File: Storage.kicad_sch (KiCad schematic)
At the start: 12 parts, among them U5 KLM4G1FETE-B041

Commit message: changed some ethernet stuff
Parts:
- gave numbers to parts that had none: 1
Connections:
- net EMMC_CMD: now also U1.E16 (PC6/NAND_RB0)
- net EMMC_DQ0: now also U1.B18 (PC8/NAND_DQ0)
- net EMMC_DQ1: now also U1.C17 (PC9/NAND_DQ1)
- net EMMC_DQ2: now also U1.D17 (PC10/NAND_DQ2)
- net EMMC_DQ3: now also U1.C18 (PC11/NAND_DQ3)
- net EMMC_DQ4: now also U1.B17 (PC12/NAND_DQ4)
- net EMMC_DQ5: now also U1.B19 (PC13/NAND_DQ5)
- net EMMC_DQ6: now also U1.F17 (PC14/NAND_DQ6)
- net EMMC_DQ7: now also U1.C19 (PC15/NAND_DQ7)
- net EMMC_RST: now also U1.H16 (PC16/NAND_DQS)
- net at R5.1: now also U1.A17 (PC5/NAND_RE)
- new net SPI0_CLK: U1.B16 (PC2/NAND_CLE)
- new net SPI0_CS: U1.B15 (PC3/NAND_CE1)
- new net SPI0_MISO: U1.C16 (PC1/NAND_ALE)
- new net SPI0_MOSI: U1.C15 (PC0/NAND_WE)
- no-connect marks 127 -> 123
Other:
- moved on the sheet: R5

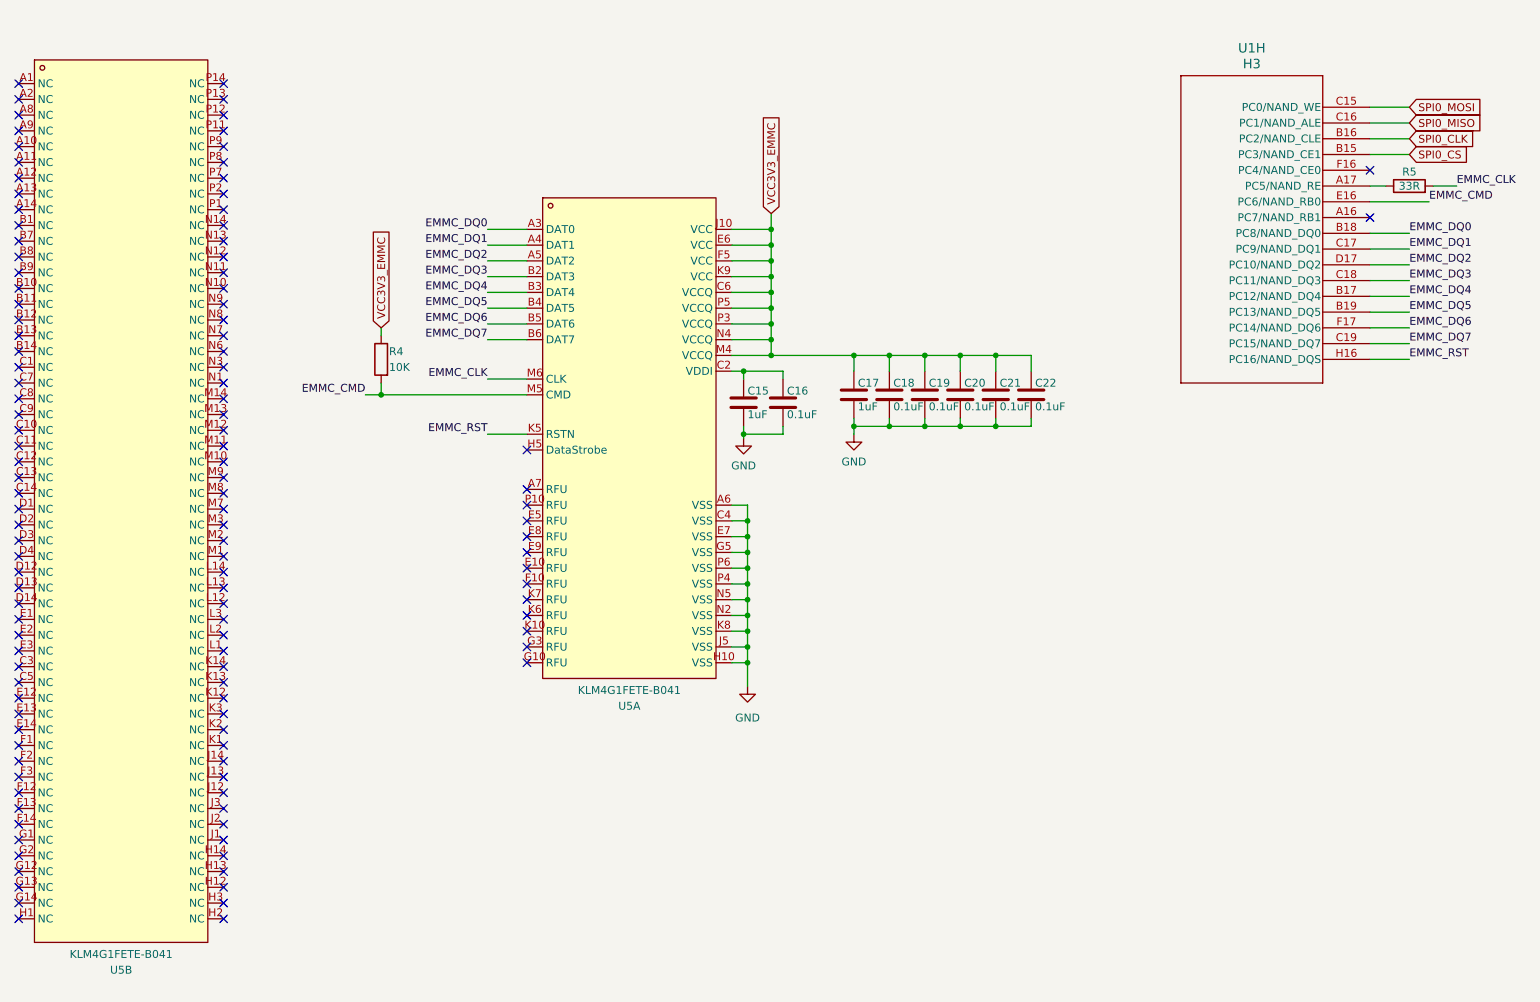
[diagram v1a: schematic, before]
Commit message: switched eMMC
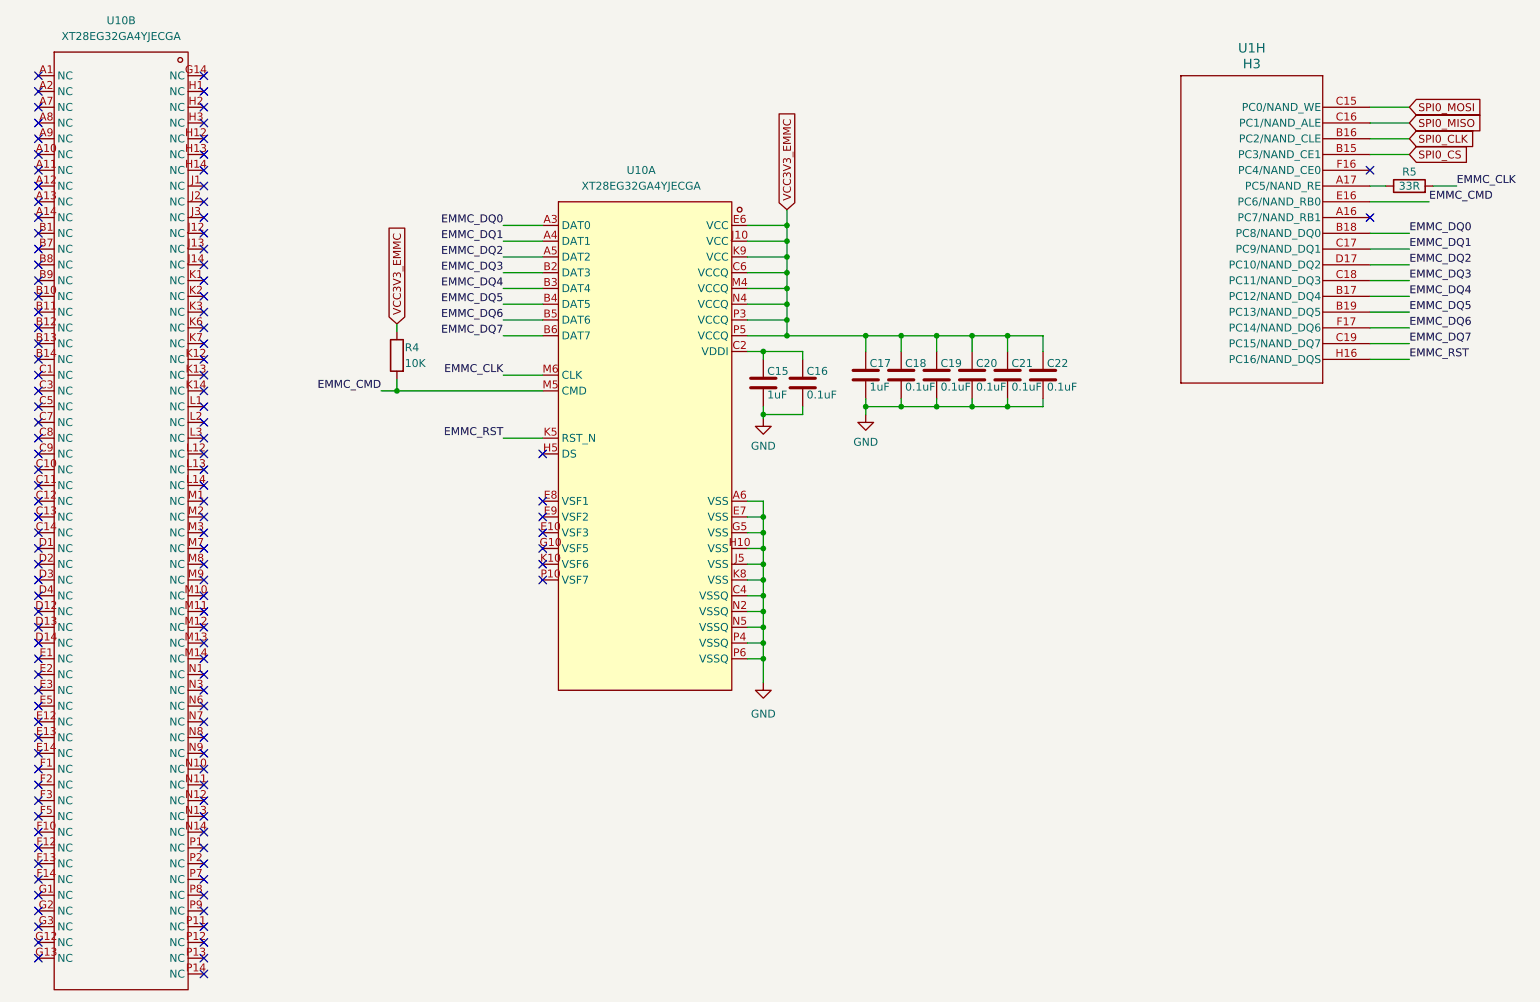
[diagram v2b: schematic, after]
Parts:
- removed U5: KLM4G1FETE-B041, easyeda2kicad:FBGA-153_L11.0-W10.0-P0.50_KLM4G1FETE-B041, symbol easyeda2kicad:KLM4G1FETE-B041
- added U10: XT28EG32GA4YJECGA, easyeda2kicad:VFBGA-153_L13.0-W11.5-P0.50-BL_SKYHIGHMEMORY_S40FC004C1B1I00000, symbol easyeda2kicad:XT28EG32GA4YJECGA
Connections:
- net EMMC_CLK: now also U10.M6 (CLK)
- net EMMC_CMD: now also U10.M5 (CMD)
- net EMMC_DQ0: now also U10.A3 (DAT0)
- net EMMC_DQ1: now also U10.A4 (DAT1)
- net EMMC_DQ2: now also U10.A5 (DAT2)
- net EMMC_DQ3: now also U10.B2 (DAT3)
- net EMMC_DQ4: now also U10.B3 (DAT4)
- net EMMC_DQ5: now also U10.B4 (DAT5)
- net EMMC_DQ6: now also U10.B5 (DAT6)
- net EMMC_DQ7: now also U10.B6 (DAT7)
- net EMMC_RST: now also U10.K5 (RST_N)
- net GND: now also U10.A6 (VSS), U10.C4 (VSSQ), U10.E7 (VSS), U10.G5 (VSS), U10.H10 (VSS), U10.J5 (VSS), U10.K8 (VSS), U10.N2 (VSSQ), U10.N5 (VSSQ), U10.P4 (VSSQ), U10.P6 (VSSQ)
- net VCC3V3_EMMC: now also U10.C6 (VCCQ), U10.E6 (VCC), U10.J10 (VCC), U10.K9 (VCC), U10.M4 (VCCQ), U10.N4 (VCCQ), U10.P3 (VCCQ), U10.P5 (VCCQ)
- net at C15.1, C16.1: now also U10.C2 (VDDI)
- no-connect marks 123 -> 124
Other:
- moved on the sheet: C15, C16, C17, C18, C19, C20, C21, C22, R4

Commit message: minor changes
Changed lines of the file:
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@@
 		(dnp no)
 		(property "Reference" "U1"
-			(at 233.68 33.655 0)
+			(at 223.52 35.56 0)
 			(effects
 				(font
@@
 		)
 		(property "Value" "H3"
-			(at 233.68 36.195 0)
+			(at 223.52 38.1 0)
 			(effects
 				(font
@@
 		)
 		(instances
-			(project "H3_SBC"
+			(project ""
+				(path "/2511caf5-b791-49bc-bcf7-734707cf883b"
+					(reference "U1")
+					(unit 8)
+				)
 				(path "/2511caf5-b791-49bc-bcf7-734707cf883b/7c195a19-3b4b-4cd4-badd-fe195946fa30"
 					(reference "U1")

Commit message: linking symbols to footprints
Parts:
- C15, C17: footprint (none) -> Capacitor_SMD:C_0402_1005Metric
- C16, C18, C19, C20, C21, C22: footprint (none) -> Capacitor_SMD:C_0603_1608Metric
- R4, R5: footprint (none) -> Resistor_SMD:R_0402_1005Metric
- U1: footprint BGA347_H3_AWT -> (none)
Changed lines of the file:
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@@
 			)
 		)
-		(property "Footprint" ""
+		(property "Footprint" "Capacitor_SMD:C_0402_1005Metric"
 			(at 155.9052 91.44 0)
 			(effects
@@
 			)
 		)
-		(property "Footprint" ""
+		(property "Footprint" "Capacitor_SMD:C_0603_1608Metric"
 			(at 195.2752 90.17 0)
 			(effects
@@
 			)
 		)
-		(property "Footprint" ""
+		(property "Footprint" "Capacitor_SMD:C_0603_1608Metric"
 			(at 200.9902 90.17 0)
 			(effects
@@
 			)
 		)
-		(property "Footprint" ""
+		(property "Footprint" "Resistor_SMD:R_0402_1005Metric"
 			(at 97.663 83.185 90)
 			(effects
@@
 			)
 		)
-		(property "Footprint" ""
+		(property "Footprint" "Capacitor_SMD:C_0603_1608Metric"
 			(at 162.2552 91.44 0)
 			(effects
@@
 			)
 		)
-		(property "Footprint" ""
+		(property "Footprint" "Capacitor_SMD:C_0603_1608Metric"
 			(at 189.5602 90.17 0)
 			(effects
@@
 			)
 		)
-		(property "Footprint" ""
+		(property "Footprint" "Capacitor_SMD:C_0402_1005Metric"
 			(at 172.4152 90.17 0)
 			(effects
@@
 			)
 		)
-		(property "Footprint" "BGA347_H3_AWT"
+		(property "Footprint" ""
 			(at 200.66 45.72 0)
 			(effects
@@
 			)
 		)
-		(property "Footprint" ""
+		(property "Footprint" "Capacitor_SMD:C_0603_1608Metric"
 			(at 183.8452 90.17 0)
 			(effects
@@
 			)
 		)
-		(property "Footprint" ""
+		(property "Footprint" "Capacitor_SMD:C_0603_1608Metric"
 			(at 178.1302 90.17 0)
 			(effects
@@
 			)
 		)
-		(property "Footprint" ""
+		(property "Footprint" "Resistor_SMD:R_0402_1005Metric"
 			(at 259.08 57.658 90)
 			(effects

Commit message: placed major components
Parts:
- C16, C18, C19, C20, C21, C22: footprint Capacitor_SMD:C_0603_1608Metric -> Capacitor_SMD:C_0402_1005Metric
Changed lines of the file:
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@@
 			)
 		)
-		(property "Footprint" "Capacitor_SMD:C_0603_1608Metric"
+		(property "Footprint" "Capacitor_SMD:C_0402_1005Metric"
 			(at 195.2752 90.17 0)
 			(effects
@@
 			)
 		)
-		(property "Footprint" "Capacitor_SMD:C_0603_1608Metric"
+		(property "Footprint" "Capacitor_SMD:C_0402_1005Metric"
 			(at 200.9902 90.17 0)
 			(effects
@@
 			)
 		)
-		(property "Footprint" "Capacitor_SMD:C_0603_1608Metric"
+		(property "Footprint" "Capacitor_SMD:C_0402_1005Metric"
 			(at 162.2552 91.44 0)
 			(effects
@@
 			)
 		)
-		(property "Footprint" "Capacitor_SMD:C_0603_1608Metric"
+		(property "Footprint" "Capacitor_SMD:C_0402_1005Metric"
 			(at 189.5602 90.17 0)
 			(effects
@@
 			)
 		)
-		(property "Footprint" "Capacitor_SMD:C_0603_1608Metric"
+		(property "Footprint" "Capacitor_SMD:C_0402_1005Metric"
 			(at 183.8452 90.17 0)
 			(effects
@@
 			)
 		)
-		(property "Footprint" "Capacitor_SMD:C_0603_1608Metric"
+		(property "Footprint" "Capacitor_SMD:C_0402_1005Metric"
 			(at 178.1302 90.17 0)
 			(effects

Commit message: started RAM routing, might move to 1 module though
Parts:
- U1: footprint (none) -> easyeda2kicad:BGA-347_L14.0-W14.0-R21-C21-P0.65-TL
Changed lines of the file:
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@@
 			)
 		)
-		(property "Footprint" ""
+		(property "Footprint" "easyeda2kicad:BGA-347_L14.0-W14.0-R21-C21-P0.65-TL"
 			(at 200.66 45.72 0)
 			(effects
